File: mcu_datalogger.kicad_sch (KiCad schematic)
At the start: 0 parts

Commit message: Added symbols in 2 sheets
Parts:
- added BT1: Battery_Cell, symbol Device:Battery_Cell
- added C1, C2, C3, C4: C, symbol Device:C
- added C5: C_Polarized, symbol Device:C_Polarized
- added D1, D2: LED, symbol Device:LED
- added H1, H2, H3, H4: MountingHole, symbol Mechanical:MountingHole
- added R1, R2, R3, R4, R5, R6, R7: R, symbol Device:R
- added U1: DS1337S_, DS1337S_:SOIC127P600X175-8N, symbol DS1337S_:DS1337S_
- added U2: ATMEGA328P-AU, ATMEGA328P-AU:QFP80P900X900X120-32N, symbol ATMEGA328P-AU:ATMEGA328P-AU
- added U3, U4: 24LC1025, symbol Memory_EEPROM:24LC1025
- added Y1, Y2: Crystal, symbol Device:Crystal
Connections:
- new net: U2.21 (GND), U2.3 (GND), U2.5 (GND)
- new net: U2.4 (VCC), U2.6 (VCC)
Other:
- added sheet connectors (connectors_sheet.kicad_sch)

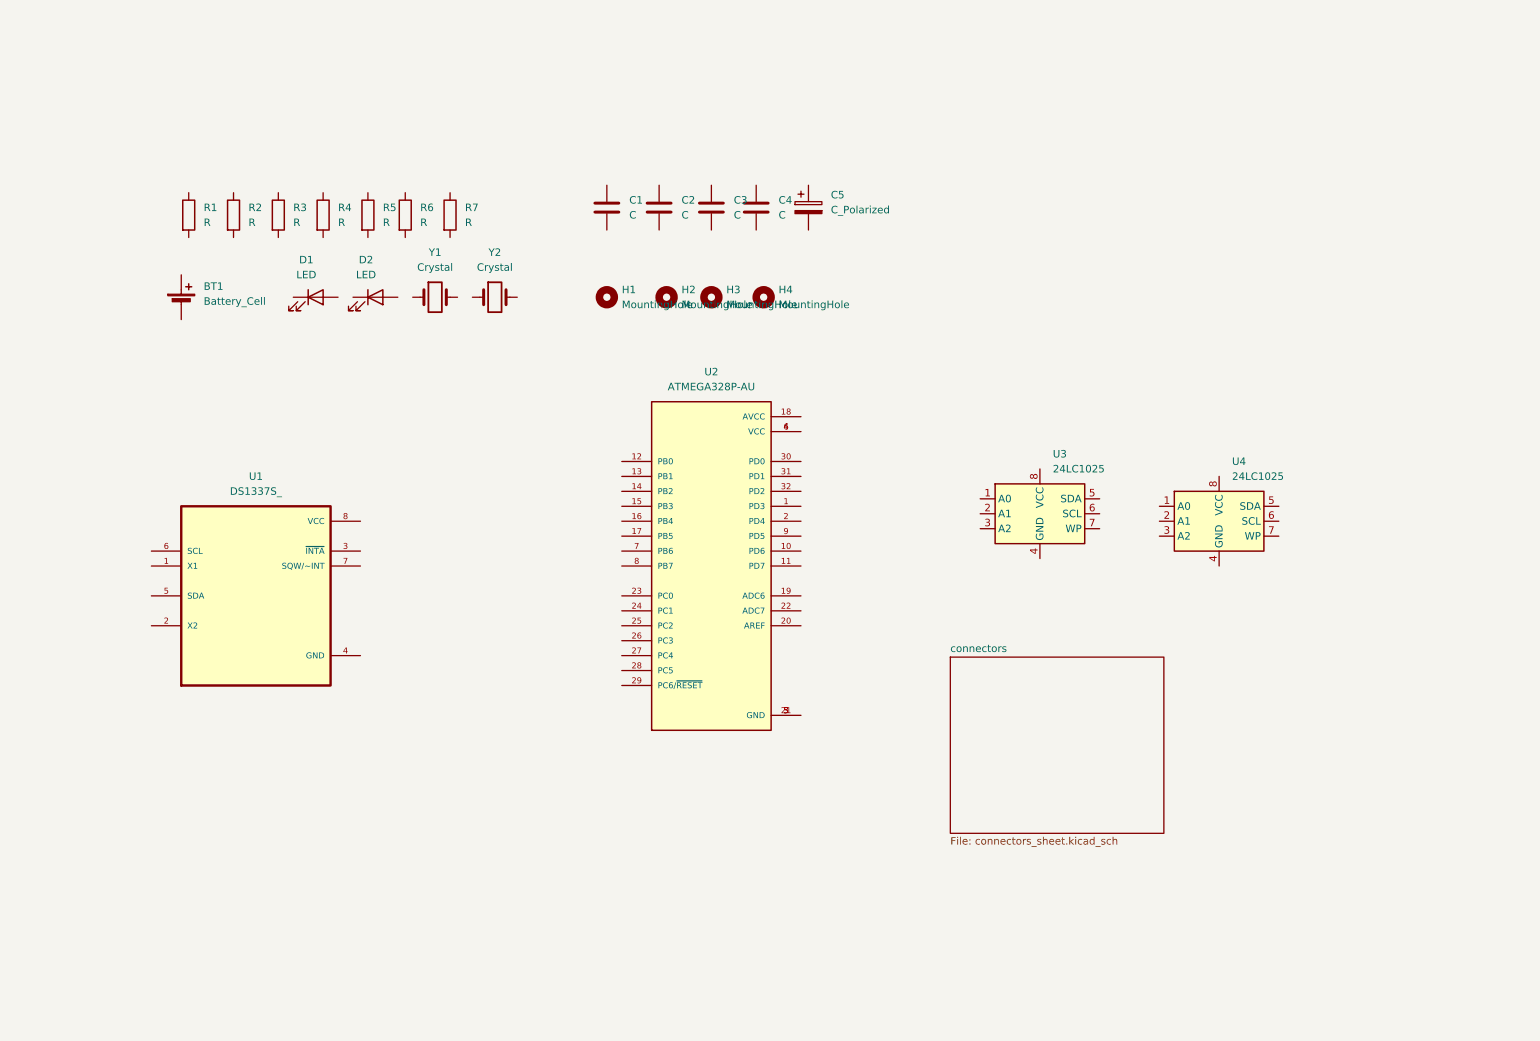
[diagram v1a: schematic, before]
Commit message: Changed locations of symbols
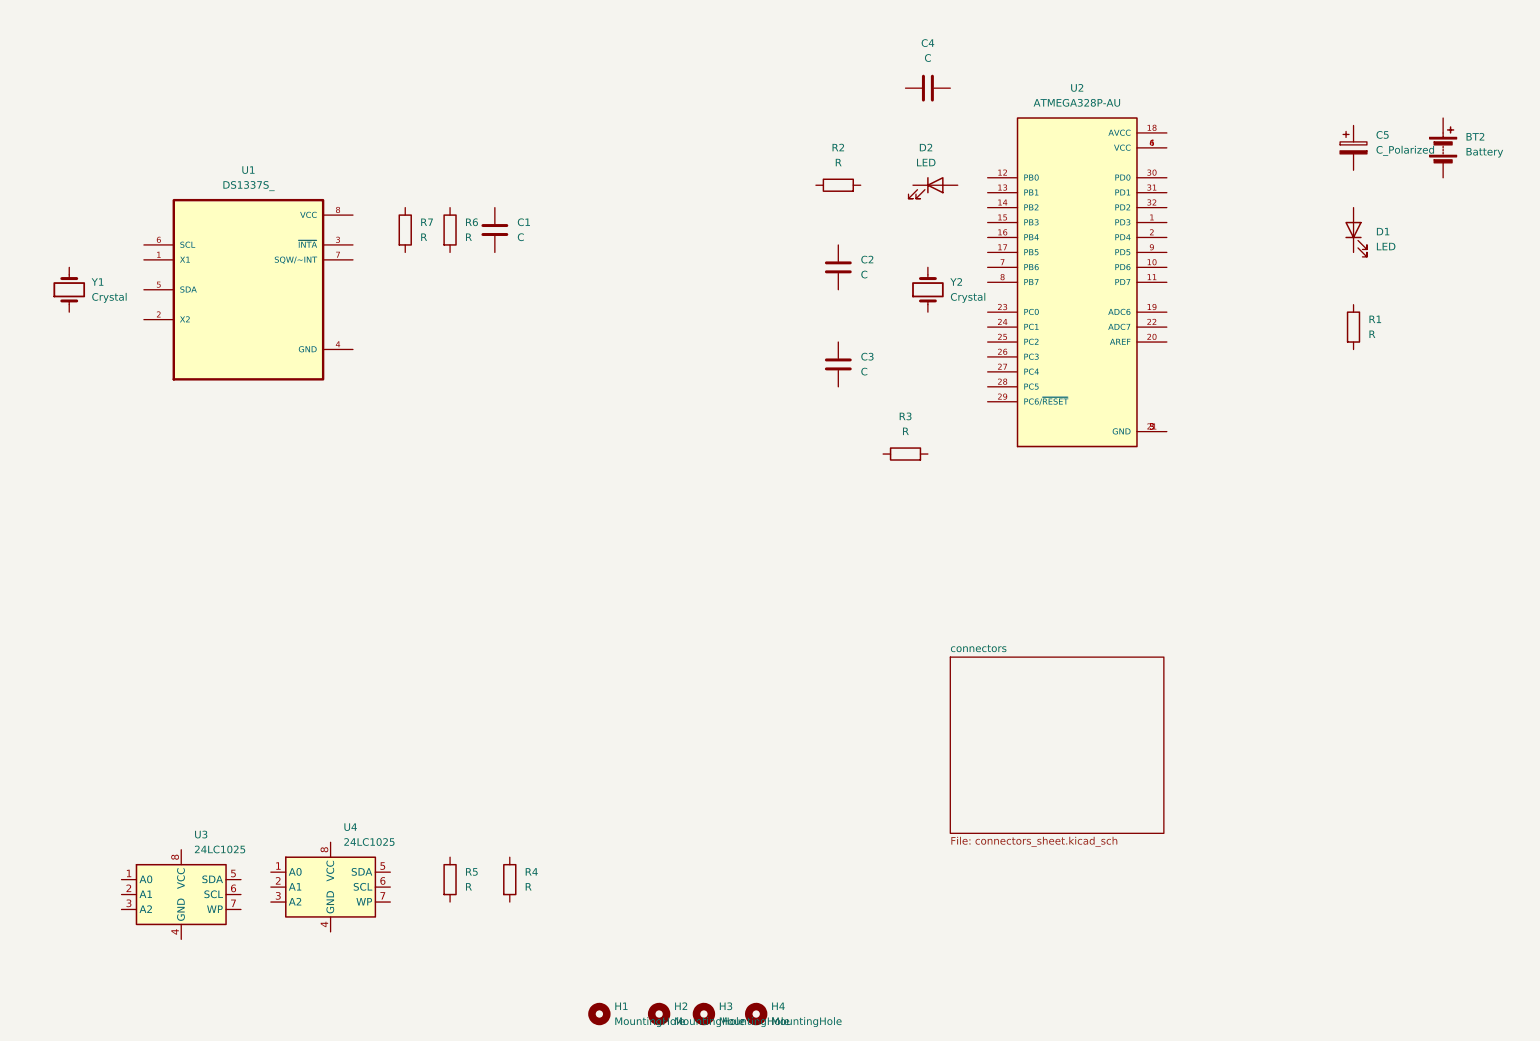
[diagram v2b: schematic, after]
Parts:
- removed BT1: Battery_Cell, symbol Device:Battery_Cell
- added BT2: Battery, symbol Device:Battery
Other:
- moved on the sheet: C1, C2, C3, C4, C5, D1, D2, H1, H2, H3, H4, R1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

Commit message: Added Component Values
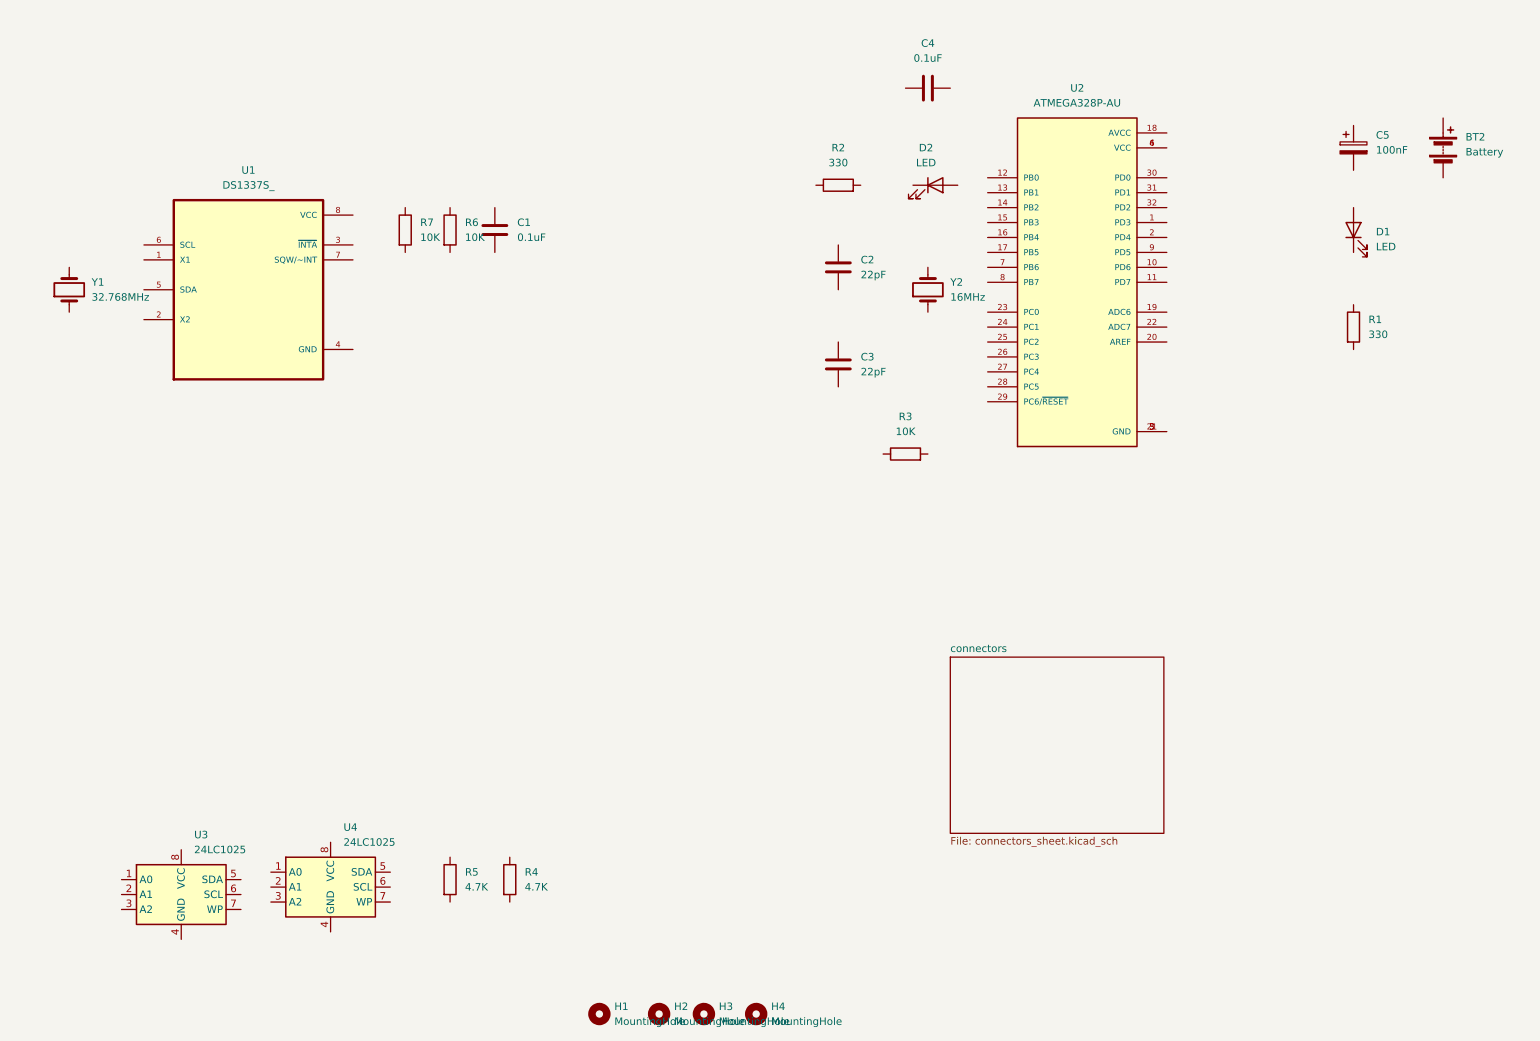
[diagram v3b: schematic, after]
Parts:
- C1, C4: value C -> 0.1uF
- C2, C3: value C -> 22pF
- C5: value C_Polarized -> 100nF
- R1, R2: value R -> 330
- R3, R6, R7: value R -> 10K
- R4, R5: value R -> 4.7K
- Y1: value Crystal -> 32.768MHz
- Y2: value Crystal -> 16MHz
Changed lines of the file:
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@@
 			)
 		)
-		(property "Value" "R"
+		(property "Value" "4.7K"
 			(at 99.06 167.6399 0)
 			(effects
@@
 			)
 		)
-		(property "Value" "R"
+		(property "Value" "4.7K"
 			(at 109.22 167.6399 0)
 			(effects
@@
 			)
 		)
-		(property "Value" "Crystal"
+		(property "Value" "32.768MHz"
 			(at 35.56 67.3099 90)
 			(effects
@@
 			)
 		)
-		(property "Value" "R"
+		(property "Value" "330"
 			(at 162.56 44.45 90)
 			(effects
@@
 			)
 		)
-		(property "Value" "C"
+		(property "Value" "0.1uF"
 			(at 177.8 26.67 90)
 			(effects
@@
 			)
 		)
-		(property "Value" "C"
+		(property "Value" "22pF"
 			(at 166.37 63.4999 0)
 			(effects
@@
 			)
 		)
-		(property "Value" "R"
+		(property "Value" "330"
 			(at 252.73 73.6599 0)
 			(effects
@@
 			)
 		)
-		(property "Value" "C"
+		(property "Value" "0.1uF"
 			(at 107.95 57.1499 0)
 			(effects
@@
 			)
 		)
-		(property "Value" "R"
+		(property "Value" "10K"
 			(at 173.99 90.17 90)
 			(effects
@@
 			)
 		)
-		(property "Value" "Crystal"
+		(property "Value" "16MHz"
 			(at 181.61 67.3099 90)
 			(effects
@@
 			)
 		)
-		(property "Value" "R"
+		(property "Value" "10K"
 			(at 99.06 57.1499 0)
 			(effects
@@
 			)
 		)
-		(property "Value" "C"
+		(property "Value" "22pF"
 			(at 166.37 80.0099 0)
 			(effects
@@
 			)
 		)
-		(property "Value" "C_Polarized"
+		(property "Value" "100nF"
 			(at 254 42.2909 0)
 			(effects
@@
 			)
 		)
-		(property "Value" "R"
+		(property "Value" "10K"
 			(at 91.44 57.1499 0)
 			(effects

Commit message: Updated the Footprint
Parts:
- BT2: footprint (none) -> Connector_PinHeader_2.54mm:PinHeader_1x02_P2.54mm_Vertical
- C1, C2, C3, C4: footprint (none) -> Capacitor_SMD:C_0805_2012Metric
- C5, D1, D2: footprint (none) -> LED_SMD:LED_0805_2012Metric
- H1, H2, H3, H4: footprint (none) -> MountingHole:MountingHole_2.1mm
- R1, R2, R3, R4, R5, R6, R7: footprint (none) -> Resistor_SMD:R_0805_2012Metric
- U3, U4: footprint (none) -> Package_SO:SOIC-8_5.23x5.23mm_P1.27mm
- Y1, Y2: footprint (none) -> Crystal:Crystal_SMD_5032-2Pin_5.0x3.2mm_HandSoldering
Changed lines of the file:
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@@
 			)
 		)
-		(property "Footprint" ""
+		(property "Footprint" "LED_SMD:LED_0805_2012Metric"
 			(at 250.19 55.88 0)
 			(effects
@@
 			)
 		)
-		(property "Footprint" ""
+		(property "Footprint" "Resistor_SMD:R_0805_2012Metric"
 			(at 94.742 166.37 90)
 			(effects
@@
 			)
 		)
-		(property "Footprint" ""
+		(property "Footprint" "MountingHole:MountingHole_2.1mm"
 			(at 132.08 189.23 0)
 			(effects
@@
 			)
 		)
-		(property "Footprint" ""
+		(property "Footprint" "Resistor_SMD:R_0805_2012Metric"
 			(at 104.902 166.37 90)
 			(effects
@@
 			)
 		)
-		(property "Footprint" ""
+		(property "Footprint" "Package_SO:SOIC-8_5.23x5.23mm_P1.27mm"
 			(at 50.8 168.91 0)
 			(effects
@@
 			)
 		)
-		(property "Footprint" ""
+		(property "Footprint" "MountingHole:MountingHole_2.1mm"
 			(at 148.59 189.23 0)
 			(effects
@@
 			)
 		)
-		(property "Footprint" ""
+		(property "Footprint" "MountingHole:MountingHole_2.1mm"
 			(at 139.7 189.23 0)
 			(effects
@@
 			)
 		)
-		(property "Footprint" ""
+		(property "Footprint" "Package_SO:SOIC-8_5.23x5.23mm_P1.27mm"
 			(at 76.2 167.64 0)
 			(effects
@@
 			)
 		)
-		(property "Footprint" ""
+		(property "Footprint" "Crystal:Crystal_SMD_5032-2Pin_5.0x3.2mm_HandSoldering"
 			(at 31.75 66.04 0)
 			(effects
@@
 			)
 		)
-		(property "Footprint" ""
+		(property "Footprint" "Resistor_SMD:R_0805_2012Metric"
 			(at 162.56 50.038 90)
 			(effects
@@
 			)
 		)
-		(property "Footprint" ""
+		(property "Footprint" "MountingHole:MountingHole_2.1mm"
 			(at 121.92 189.23 0)
 			(effects
@@
 			)
 		)
-		(property "Footprint" ""
+		(property "Footprint" "Capacitor_SMD:C_0805_2012Metric"
 			(at 181.61 30.7848 0)
 			(effects
@@
 			)
 		)
-		(property "Footprint" ""
+		(property "Footprint" "Capacitor_SMD:C_0805_2012Metric"
 			(at 163.5252 66.04 0)
 			(effects
@@
 			)
 		)
-		(property "Footprint" ""
+		(property "Footprint" "Resistor_SMD:R_0805_2012Metric"
 			(at 248.412 72.39 90)
 			(effects
@@
 			)
 		)
-		(property "Footprint" ""
+		(property "Footprint" "Capacitor_SMD:C_0805_2012Metric"
 			(at 105.1052 59.69 0)
 			(effects
@@
 			)
 		)
-		(property "Footprint" ""
+		(property "Footprint" "Connector_PinHeader_2.54mm:PinHeader_1x02_P2.54mm_Vertical"
 			(at 265.43 40.386 90)
 			(effects
@@
 			)
 		)
-		(property "Footprint" ""
+		(property "Footprint" "Resistor_SMD:R_0805_2012Metric"
 			(at 173.99 95.758 90)
 			(effects
@@
 			)
 		)
-		(property "Footprint" ""
+		(property "Footprint" "Crystal:Crystal_SMD_5032-2Pin_5.0x3.2mm_HandSoldering"
 			(at 177.8 66.04 0)
 			(effects
@@
 			)
 		)
-		(property "Footprint" ""
+		(property "Footprint" "Resistor_SMD:R_0805_2012Metric"
 			(at 94.742 55.88 90)
 			(effects
@@
 			)
 		)
-		(property "Footprint" ""
+		(property "Footprint" "Capacitor_SMD:C_0805_2012Metric"
 			(at 163.5252 82.55 0)
 			(effects
@@
 			)
 		)
-		(property "Footprint" ""
+		(property "Footprint" "LED_SMD:LED_0805_2012Metric"
 			(at 251.1552 45.72 0)
 			(effects
@@
 			)
 		)
-		(property "Footprint" ""
+		(property "Footprint" "LED_SMD:LED_0805_2012Metric"
 			(at 179.07 48.26 0)
 			(effects
@@
 			)
 		)
-		(property "Footprint" ""
+		(property "Footprint" "Resistor_SMD:R_0805_2012Metric"
 			(at 87.122 55.88 90)
 			(effects
